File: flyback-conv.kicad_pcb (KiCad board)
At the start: 2 copper layers, 1 part

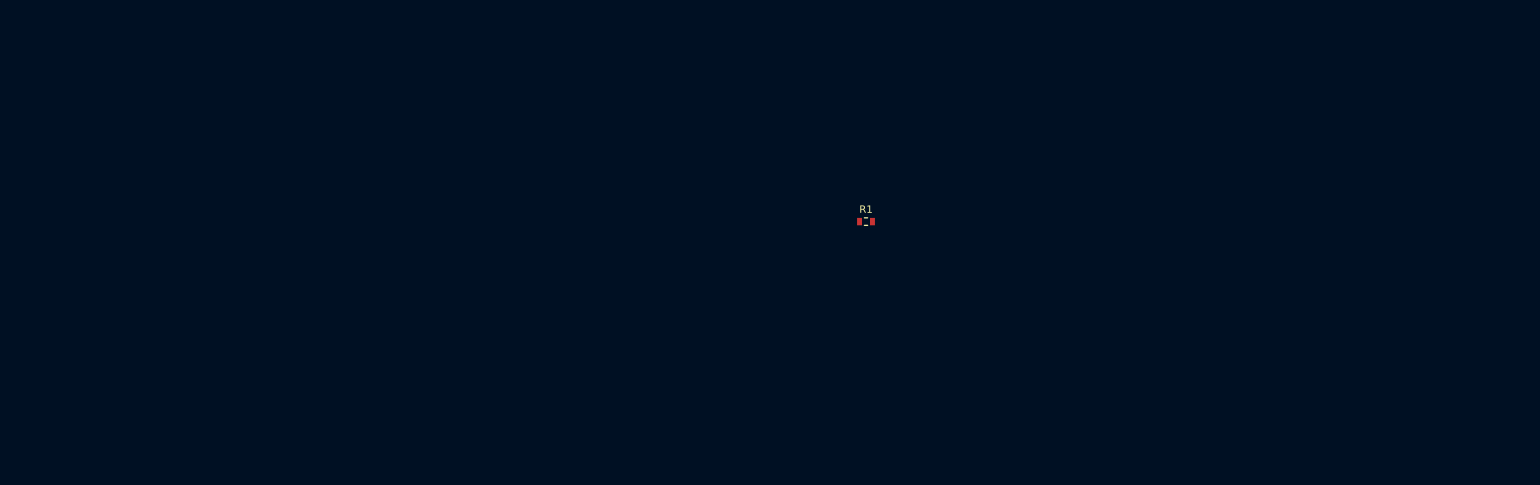
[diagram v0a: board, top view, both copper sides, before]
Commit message: fixed few lib componentes and screated PCB
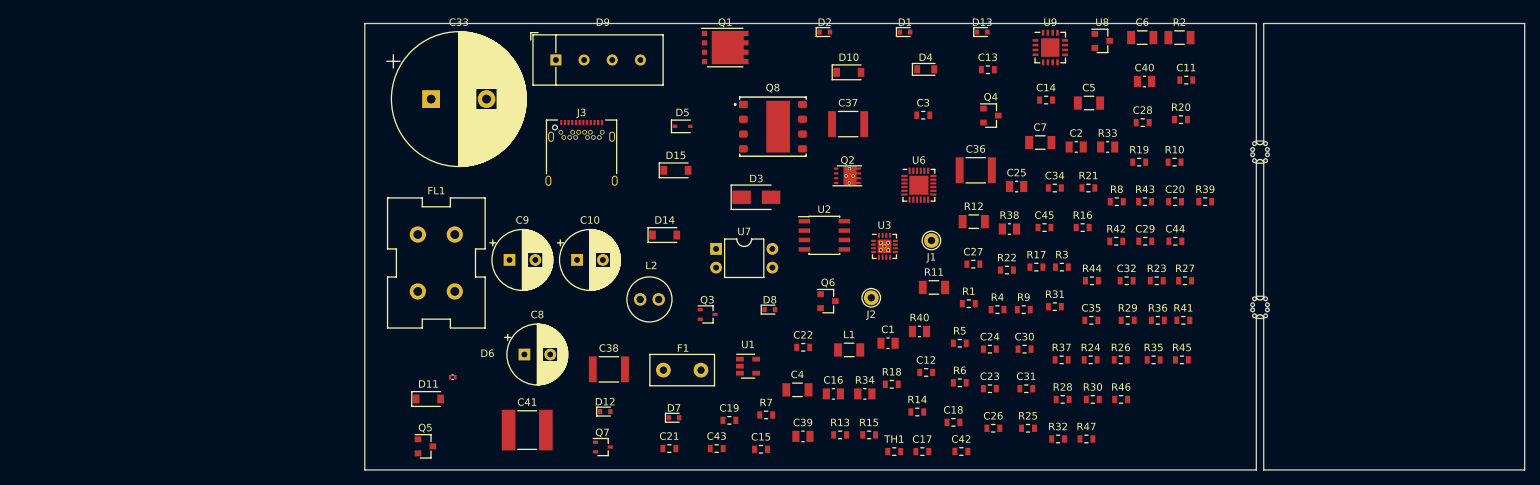
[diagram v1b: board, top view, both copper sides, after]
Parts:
- added C1: 2.2uF, Capacitor_SMD:C_0805_2012Metric, F.Cu at (173.6, 102.3)
- added C10: 270uF, Capacitor_THT:CP_Radial_D8.0mm_P3.50mm, F.Cu at (131.5, 91.0)
- added C11: 0.01uF, Capacitor_SMD:C_0603_1608Metric, F.Cu at (213.9, 66.7)
- added C12: 0.33uF, Capacitor_SMD:C_0603_1608Metric, F.Cu at (178.7, 106.2)
- added C13: 0.022uF, Capacitor_SMD:C_0603_1608Metric, F.Cu at (187.1, 65.3)
- added C14: 0.022uF, Capacitor_SMD:C_0603_1608Metric, F.Cu at (195.0, 69.4)
- added C15: 2200pF, Capacitor_SMD:C_0603_1608Metric, F.Cu at (156.4, 116.6)
- added C16: 6.8uF, Capacitor_SMD:C_0805_2012Metric, F.Cu at (166.2, 109.1)
- added C17: 12pF, Capacitor_SMD:C_0603_1608Metric, F.Cu at (178.2, 116.9)
- added C18: 22pF, Capacitor_SMD:C_0603_1608Metric, F.Cu at (182.4, 113.0)
- added C19: 0.022uF, Capacitor_SMD:C_0603_1608Metric, F.Cu at (152.1, 112.7)
- added C2: 2.2uF, Capacitor_SMD:C_0805_2012Metric, F.Cu at (199.0, 75.7)
- added C20: 3.3pF, Capacitor_SMD:C_0603_1608Metric, F.Cu at (212.4, 83.1)
- added C21: 0.022uF, Capacitor_SMD:C_0603_1608Metric, F.Cu at (144.0, 116.5)
- added C22: 0.022uF, Capacitor_SMD:C_0603_1608Metric, F.Cu at (162.1, 102.8)
- added C23: 0.1uF, Capacitor_SMD:C_0603_1608Metric, F.Cu at (187.4, 108.4)
- added C24: 0.1uF, Capacitor_SMD:C_0603_1608Metric, F.Cu at (187.4, 103.1)
- added C25: 4.7uF, Capacitor_SMD:C_0805_2012Metric, F.Cu at (191.0, 81.1)
- added C26: 0.1uF, Capacitor_SMD:C_0603_1608Metric, F.Cu at (187.8, 113.8)
- added C27: 0.01uF, Capacitor_SMD:C_0603_1608Metric, F.Cu at (185.1, 91.6)
- added C28: 0.01uF, Capacitor_SMD:C_0603_1608Metric, F.Cu at (208.0, 72.4)
- added C29: 1uF, Capacitor_SMD:C_0603_1608Metric, F.Cu at (208.4, 88.5)
- added C3: 220pF/250V, Capacitor_SMD:C_0603_1608Metric, F.Cu at (178.3, 71.4)
- added C30: 0.1uF, Capacitor_SMD:C_0603_1608Metric, F.Cu at (192.0, 103.1)
- added C31: 220pF, Capacitor_SMD:C_0603_1608Metric, F.Cu at (192.3, 108.4)
- added C32: 0.1uF, Capacitor_SMD:C_0603_1608Metric, F.Cu at (205.9, 93.8)
- added C33: 82uF, Capacitor_THT:CP_Radial_D18.0mm_P7.50mm, F.Cu at (111.8, 69.2)
- added C34: 0.22uF, Capacitor_SMD:C_0603_1608Metric, F.Cu at (196.1, 81.3)
- added C35: 220pF, Capacitor_SMD:C_0603_1608Metric, F.Cu at (201.1, 99.2)
- added C36: 0.47uF, Capacitor_SMD:C_1812_4532Metric, F.Cu at (185.4, 78.9)
- added C37: 0.22uF/500V, Capacitor_SMD:C_1812_4532Metric, F.Cu at (168.2, 72.6)
- added C38: 0.22uF/500V, Capacitor_SMD:C_1812_4532Metric, F.Cu at (135.8, 105.8)
- added C39: 0.47uF, Capacitor_SMD:C_0805_2012Metric, F.Cu at (162.1, 114.9)
- added C4: 33uF, Capacitor_SMD:C_1206_3216Metric, F.Cu at (161.3, 108.6)
- added C40: 0.47uF, Capacitor_SMD:C_0805_2012Metric, F.Cu at (208.3, 66.9)
- added C41: 2200pF/250V, Capacitor_SMD:C_2220_5650Metric, F.Cu at (124.8, 114.0)
- added C42: 560pF, Capacitor_SMD:C_0603_1608Metric, F.Cu at (183.5, 116.9)
- added C43: 4700pF, Capacitor_SMD:C_0603_1608Metric, F.Cu at (150.4, 116.5)
- added C44: 3.3pF, Capacitor_SMD:C_0603_1608Metric, F.Cu at (212.4, 88.5)
- added C45: 0.01uF, Capacitor_SMD:C_0603_1608Metric, F.Cu at (194.7, 86.6)
- added C5: 33uF, Capacitor_SMD:C_1206_3216Metric, F.Cu at (200.8, 69.8)
- added C6: 10uF, Capacitor_SMD:C_1206_3216Metric, F.Cu at (208.0, 60.9)
- added C7: 10uF, Capacitor_SMD:C_1206_3216Metric, F.Cu at (194.2, 75.1)
- added C8: 270uF, Capacitor_THT:CP_Radial_D8.0mm_P3.50mm, F.Cu at (124.4, 103.8)
- added C9: 270uF, Capacitor_THT:CP_Radial_D8.0mm_P3.50mm, F.Cu at (122.4, 91.0)
- added D1: SDM03U40-7, Diode_SMD:D_SOD-523, F.Cu at (175.9, 60.2)
- added D10: BAV21W-7-F, Diode_SMD:D_SOD-123, F.Cu at (168.3, 65.6)
- added D11: MMSZ5248B-7-F, Diode_SMD:D_SOD-123, F.Cu at (111.4, 109.8)
- added D12: CZRU52C6V2, Diode_SMD:D_SOD-523, F.Cu at (135.3, 111.5)
- added D13: CZRU52C6V2, Diode_SMD:D_SOD-523, F.Cu at (186.3, 60.2)
- added D14: CSFMT108-HF, Diode_SMD:D_SOD-123, F.Cu at (143.4, 87.6)
- added D15: CSFMT108-HF, Diode_SMD:D_SOD-123, F.Cu at (144.9, 78.9)
- added D2: BZT52C22T-7, Diode_SMD:D_SOD-523, F.Cu at (165.0, 60.2)
- added D3: B340A-13-F, Diode_SMD:D_SMA, F.Cu at (155.8, 82.5)
- added D4: RFU02VSM6S, custom-lib:TUMD2SM, F.Cu at (178.7, 65.2)
- added D5: CDSOD323-T24S, Diode_SMD:D_SOD-323, F.Cu at (145.8, 72.9)
- added D6: TPD1E05U06QDPYRQ, custom-lib:X1SON2, F.Cu at (114.7, 106.8)
- added D7: CZRU52C2, Diode_SMD:D_SOD-523, F.Cu at (144.6, 112.3)
- added D8: CZRU52C2, Diode_SMD:D_SOD-523, F.Cu at (157.6, 97.7)
- added D9: KBP06G, custom-lib:VISHAY_2KBP, F.Cu at (128.7, 63.9)
- added F1: Fuse, Fuse:Fuse_Littlefuse_395Series, F.Cu at (143.2, 105.9)
- added FL1: 20mH, Inductor_THT:L_CommonMode_Wuerth_WE-CMB-S, F.Cu at (110.0, 87.5)
- added J1: HOLE, Connector_Pin:Pin_D1.0mm_L10.0mm, F.Cu at (179.4, 88.4)
- added J2: HOLE, Connector_Pin:Pin_D1.0mm_L10.0mm, F.Cu at (171.3, 96.1)
- added J3: USB_C_Receptacle, Connector_USB:USB_C_Receptacle_Amphenol_12401548E4-2A, F.Cu at (132.1, 77.4)
- added L1: 0.68uH, Inductor_SMD:L_1206_3216Metric, F.Cu at (168.3, 103.2)
- added L2: 1uH, custom-lib:WURTH_7447462010, F.Cu at (140.1, 96.3)
- added Q1: BSC093N15NS5ATMA, Package_SON:VSONP-8-1EP_5x6_P1.27mm, F.Cu at (151.6, 62.3)
- added Q2: CSD17578Q3, custom-lib:VSONP-8-1EP_3.3x3.3_P0.65mm, F.Cu at (168.1, 79.6)
- added Q3: 2N7002KW, Package_TO_SOT_SMD:SOT-323_SC-70, F.Cu at (149.2, 98.4)
- added Q4: DMP510DL, Package_TO_SOT_SMD:SOT-23, F.Cu at (187.5, 71.5)
- added Q5: BSS126H6906, Package_TO_SOT_SMD:SOT-23, F.Cu at (111.0, 116.2)
- added Q6: MMBTA42, Package_TO_SOT_SMD:SOT-23, F.Cu at (165.5, 96.6)
- added Q7: 2N7002KW, Package_TO_SOT_SMD:SOT-323_SC-70, F.Cu at (135.0, 116.3)
- added Q8: PGA26E07, custom-lib:PANASONIC_PGA26E07BA, F.Cu at (158.0, 73.0)
- added R10: 24.9R, Resistor_SMD:R_0603_1608Metric, F.Cu at (212.3, 77.8)
- added R11: 0.18R, Resistor_SMD:R_1206_3216Metric, F.Cu at (179.8, 94.7)
- added R12: 0.005R, Resistor_SMD:R_1206_3216Metric, F.Cu at (185.2, 85.8)
- added R13: 121R, Resistor_SMD:R_0603_1608Metric, F.Cu at (167.1, 114.7)
- added R14: 2R, Resistor_SMD:R_0603_1608Metric, F.Cu at (177.5, 111.6)
- added R15: 1M, Resistor_SMD:R_0603_1608Metric, F.Cu at (171.0, 114.7)
- added R16: 69.8k, Resistor_SMD:R_0603_1608Metric, F.Cu at (199.9, 86.6)
- added R17: 10k, Resistor_SMD:R_0603_1608Metric, F.Cu at (193.6, 92.0)
- added R18: 10R, Resistor_SMD:R_0603_1608Metric, F.Cu at (174.1, 107.8)
- added R19: 82.5k, Resistor_SMD:R_0603_1608Metric, F.Cu at (207.6, 77.8)
- added R2: 22R, Resistor_SMD:R_1206_3216Metric, F.Cu at (213.0, 60.9)
- added R20: 221k, Resistor_SMD:R_0603_1608Metric, F.Cu at (213.2, 72.0)
- added R21: 0R, Resistor_SMD:R_0603_1608Metric, F.Cu at (200.7, 81.3)
- added R22: 2k, Resistor_SMD:R_0603_1608Metric, F.Cu at (189.7, 92.4)
- added R23: 10R, Resistor_SMD:R_0603_1608Metric, F.Cu at (209.9, 93.8)
- added R24: 10R, Resistor_SMD:R_0603_1608Metric, F.Cu at (201.0, 104.5)
- added R25: 61.9k, Resistor_SMD:R_0603_1608Metric, F.Cu at (192.5, 113.8)
- added R26: 90.9k, Resistor_SMD:R_0603_1608Metric, F.Cu at (205.1, 104.5)
- added R27: 191k, Resistor_SMD:R_0603_1608Metric, F.Cu at (213.8, 93.8)
- added R28: 56.2k, Resistor_SMD:R_0603_1608Metric, F.Cu at (197.2, 109.9)
- added R29: 47.5k, Resistor_SMD:R_0603_1608Metric, F.Cu at (206.0, 99.2)
- added R3: 10R, Resistor_SMD:R_0603_1608Metric, F.Cu at (197.1, 92.0)
- added R30: 27k, Resistor_SMD:R_0603_1608Metric, F.Cu at (201.3, 109.9)
- added R31: 22.1k, Resistor_SMD:R_0603_1608Metric, F.Cu at (196.2, 97.3)
- added R32: 1M, Resistor_SMD:R_0603_1608Metric, F.Cu at (196.6, 115.2)
- added R33: 1M, Resistor_SMD:R_0805_2012Metric, F.Cu at (203.3, 75.7)
- added R34: 1M, Resistor_SMD:R_0805_2012Metric, F.Cu at (170.4, 109.1)
- added R35: 100k, Resistor_SMD:R_0603_1608Metric, F.Cu at (209.5, 104.5)
- added R36: 75k, Resistor_SMD:R_0603_1608Metric, F.Cu at (210.1, 99.2)
- added R37: 100R, Resistor_SMD:R_0603_1608Metric, F.Cu at (197.1, 104.5)
- added R38: 1R, Resistor_SMD:R_0805_2012Metric, F.Cu at (190.0, 86.8)
- added R39: 0R, Resistor_SMD:R_0603_1608Metric, F.Cu at (216.5, 83.1)
- added R4: 1k, Resistor_SMD:R_0603_1608Metric, F.Cu at (188.4, 97.7)
- added R40: 1R, Resistor_SMD:R_0805_2012Metric, F.Cu at (177.8, 100.7)
- added R41: 11k, Resistor_SMD:R_0603_1608Metric, F.Cu at (213.5, 99.2)
- added R42: 562R, Resistor_SMD:R_0603_1608Metric, F.Cu at (204.5, 88.5)
- added R43: 34k, Resistor_SMD:R_0603_1608Metric, F.Cu at (208.3, 83.1)
- added R44: 60.4k, Resistor_SMD:R_0603_1608Metric, F.Cu at (201.2, 93.8)
- added R45: 10R, Resistor_SMD:R_0603_1608Metric, F.Cu at (213.3, 104.5)
- added R46: 150k, Resistor_SMD:R_0603_1608Metric, F.Cu at (205.1, 109.9)
- added R47: 150k, Resistor_SMD:R_0603_1608Metric, F.Cu at (200.4, 115.2)
- added R5: 10R, Resistor_SMD:R_0603_1608Metric, F.Cu at (183.3, 102.3)
- added R6: 10R, Resistor_SMD:R_0603_1608Metric, F.Cu at (183.3, 107.6)
- added R7: 10k, Resistor_SMD:R_0603_1608Metric, F.Cu at (157.1, 112.0)
- added R8: 100k, Resistor_SMD:R_0603_1608Metric, F.Cu at (204.5, 83.1)
- added R9: 1.6k, Resistor_SMD:R_0603_1608Metric, F.Cu at (191.9, 97.7)
- added TH1: 47k, Resistor_SMD:R_0603_1608Metric, F.Cu at (174.4, 116.9)
- added U1: UCC24612, Package_TO_SOT_SMD:SOT-23-5, F.Cu at (154.6, 105.4)
- added U2: ISO7710, Package_SO:SOIC-8_3.9x4.9mm_P1.27mm, F.Cu at (165.0, 87.7)
- added U3: UCC28780, Package_DFN_QFN:QFN-16-1EP_3x3mm_P0.5mm_EP2.7x2.7mm_ThermalVias, F.Cu at (173.1, 89.2)
- added U6: TPS25740B, Package_DFN_QFN:QFN-24-1EP_4x4mm_P0.5mm_EP2.6x2.6mm, F.Cu at (177.8, 80.9)
- added U7: SFH617A-1, Package_DIP:DIP-4_W7.62mm, F.Cu at (150.3, 89.5)
- added U8: ATL431, Package_TO_SOT_SMD:SOT-23, F.Cu at (202.5, 61.4)
- added U9: AN34092B, Package_DFN_QFN:QFN-16-1EP_4x4mm_P0.65mm_EP2.5x2.5mm, F.Cu at (195.5, 62.3)
- added mouse-bite-1mm-slot: VAL**, custom-lib:mouse-bite-1mm-slot, F.Cu at (223.9, 97.4)
- added mouse-bite-1mm-slot: VAL**, custom-lib:mouse-bite-1mm-slot, F.Cu at (223.9, 76.4)
- R1: value 20k -> 100R
- moved R1 17.8 mm to (184.5, 96.9)
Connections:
- R1 pad 1: Net-(R1-Pad1) -> /F
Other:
- board outline added: 156.9 x 60.4 mm

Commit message: generated BOM v1.0, added some screenshots and added an alternative for the transformer
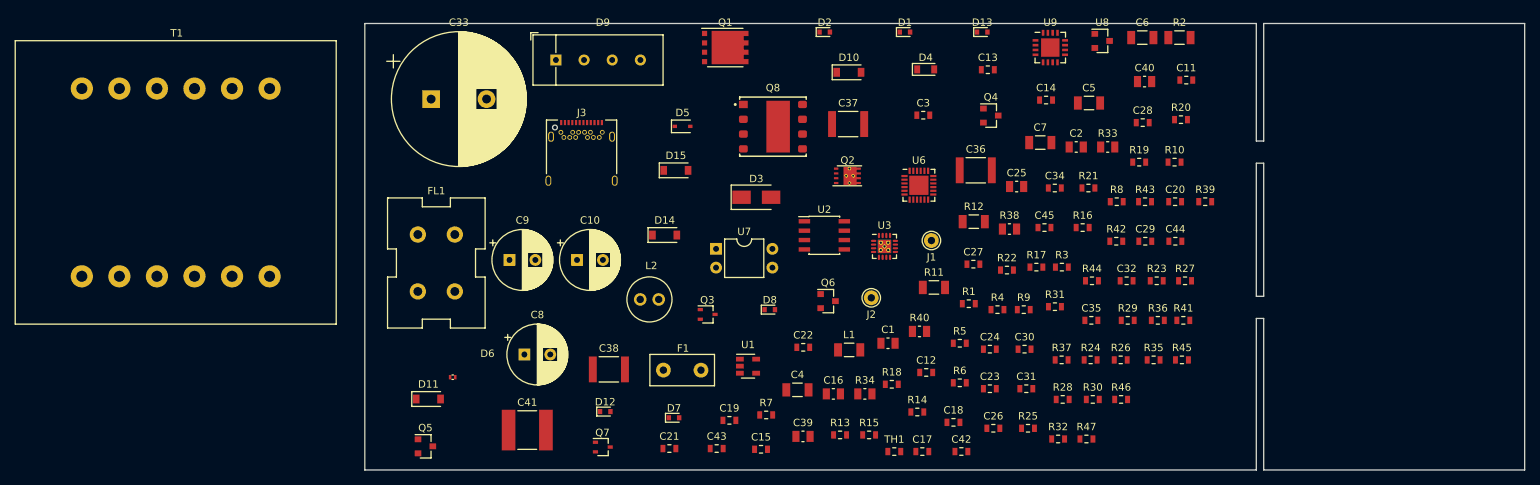
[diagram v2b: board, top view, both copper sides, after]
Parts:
- removed mouse-bite-1mm-slot (x2): VAL**, custom-lib:mouse-bite-1mm-slot
- added T1: 150-2670, Transformer_THT:Transformer_37x44, F.Cu at (69.6, 67.8)
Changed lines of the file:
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@@
   (general
     (thickness 1.6)
-    (drawings 17)
+    (drawings 18)
     (tracks 0)
     (zones 0)
-    (modules 132)
+    (modules 131)
     (nets 124)
   )
@@
     (add_net "Net-(U9-Pad9)")
   )
+  (module Transformer_THT:Transformer_37x44 (layer F.Cu)
+    (at 69.6 67.8)
+    (descr "transformer 37x44mm²")
+    (tags "transformer 37x44mm²")
+    (fp_text reference T1 (at 7.75 -7.5) (layer F.SilkS)
+      (effects (font (size 1 1) (thickness 0.15)))
+    )
+    (fp_text value 150-2670 (at 7.25 14.5) (layer F.Fab)
+      (effects (font (size 1 1) (thickness 0.15)))
+    )
+    (fp_text user %R (at 7.62 12.7) (layer F.Fab)
+      (effects (font (size 1 1) (thickness 0.15)))
+    )
+    (fp_line (start -6.99 1.27) (end 22.23 1.27) (layer F.Fab) (width 0.1))
+    (fp_line (start 22.23 1.27) (end 22.23 24.13) (layer F.Fab) (width 0.1))
+    (fp_line (start 22.23 24.13) (end -6.99 24.13) (layer F.Fab) (width 0.1))
+    (fp_line (start -6.99 24.13) (end -6.99 1.27) (layer F.Fab) (width 0.1))
+    (fp_line (start -13.97 -6.35) (end 29.21 -6.35) (layer F.Fab) (width 0.1))
+    (fp_line (start 29.21 -6.35) (end 29.21 31.75) (layer F.Fab) (width 0.1))
+    (fp_line (start 29.21 31.75) (end -13.97 31.75) (layer F.Fab) (width 0.1))
+    (fp_line (start -13.97 31.75) (end -13.97 -6.35) (layer F.Fab) (width 0.1))
+    (fp_line (start -14.22 -6.6) (end 29.46 -6.6) (layer F.CrtYd) (width 0.05))
+    (fp_line (start -14.22 -6.6) (end -14.22 32) (layer F.CrtYd) (width 0.05))
+    (fp_line (start 29.46 32) (end 29.46 -6.6) (layer F.CrtYd) (width 0.05))
+    (fp_line (start 29.46 32) (end -14.22 32) (layer F.CrtYd) (width 0.05))
+    (fp_line (start -14.09 -6.47) (end 29.33 -6.47) (layer F.SilkS) (width 0.12))
+    (fp_line (start -14.09 -6.47) (end -14.09 31.87) (layer F.SilkS) (width 0.12))
+    (fp_line (start 29.33 31.87) (end 29.33 -6.47) (layer F.SilkS) (width 0.12))
+    (fp_line (start 29.33 31.87) (end -14.09 31.87) (layer F.SilkS) (width 0.12))
+    (pad 2 thru_hole circle (at 20.32 0) (size 3 3) (drill 1.5) (layers *.Cu *.Mask)
+      (net 76 /VSW))
+    (pad 4 thru_hole circle (at -5.08 25.4) (size 3 3) (drill 1.5) (layers *.Cu *.Mask)
+      (net 8 Earth))
+    (pad 3 thru_hole circle (at 5.08 25.4) (size 3 3) (drill 1.5) (layers *.Cu *.Mask)
+      (net 58 /VS))
+    (pad 1 thru_hole circle (at 0 0) (size 3 3) (drill 1.5) (layers *.Cu *.Mask)
+      (net 11 "Net-(C33-Pad1)"))
+    (pad "" thru_hole circle (at -5.08 0) (size 3 3) (drill 1.5) (layers *.Cu *.Mask))
+    (pad "" thru_hole circle (at 5.08 0) (size 3 3) (drill 1.5) (layers *.Cu *.Mask))
+    (pad "" thru_hole circle (at 10.16 0) (size 3 3) (drill 1.5) (layers *.Cu *.Mask))
+    (pad "" thru_hole circle (at 15.24 0) (size 3 3) (drill 1.5) (layers *.Cu *.Mask))
+    (pad "" thru_hole circle (at 0 25.4) (size 3 3) (drill 1.5) (layers *.Cu *.Mask))
+    (pad "" thru_hole circle (at 10.16 25.4) (size 3 3) (drill 1.5) (layers *.Cu *.Mask))
+    (pad "" thru_hole circle (at 15.24 25.4) (size 3 3) (drill 1.5) (layers *.Cu *.Mask))
+    (pad "" thru_hole circle (at 20.32 25.4) (size 3 3) (drill 1.5) (layers *.Cu *.Mask))
+    (model ${KISYS3DMOD}/Transformer_THT.3dshapes/Transformer_37x44.wrl
+      (at (xyz 0 0 0))
+      (scale (xyz 1 1 1))
+      (rotate (xyz 0 0 0))
+    )
+    (model ${KIPRJMOD}/LIB/3D/070-4869.STEP
+      (offset (xyz -8 -28.5 0.5))
+      (scale (xyz 1 1 1))
+      (rotate (xyz -90 0 90))
+    )
+  )
   (module Capacitor_SMD:C_0603_1608Metric (layer F.Cu)
     (at 178.742619 106.2075)
@@
       (net 3 /CC2))
   )
-  (module custom-lib:mouse-bite-1mm-slot (layer F.Cu)
-    (at 223.9 97.4 90)
-    (fp_text reference mouse-bite-1mm-slot (at 0 -2 90) (layer F.SilkS) hide
-      (effects (font (size 1 1) (thickness 0.2)))
-    )
-    (fp_text value VAL** (at 0 2.1 90) (layer F.SilkS) hide
-      (effects (font (size 1 1) (thickness 0.2)))
-    )
-    (fp_line (start 1.5 0) (end 1.5 0) (layer Eco1.User) (width 1))
-    (fp_line (start -1.5 0) (end -1.5 0) (layer Eco1.User) (width 1))
-    (fp_arc (start -1.5 0) (end -1.5 -0.5) (angle 180) (layer F.SilkS) (width 0.1))
-    (fp_arc (start 1.5 0) (end 1.5 0.5) (angle 180) (layer F.SilkS) (width 0.1))
-    (fp_circle (center -1.5 0) (end -1.44 0) (layer Dwgs.User) (width 0.05))
-    (fp_circle (center 1.5 0) (end 1.56 0) (layer Dwgs.User) (width 0.05))
-    (pad "" np_thru_hole circle (at 0.35 1 90) (size 0.5 0.5) (drill 0.5) (layers *.Cu *.Mask))
-    (pad "" np_thru_hole circle (at -0.35 1 90) (size 0.5 0.5) (drill 0.5) (layers *.Cu *.Mask))
-    (pad "" np_thru_hole circle (at 1.15 -0.75 90) (size 0.5 0.5) (drill 0.5) (layers *.Cu *.Mask))
-    (pad "" np_thru_hole circle (at -0.35 -1 90) (size 0.5 0.5) (drill 0.5) (layers *.Cu *.Mask))
-    (pad "" np_thru_hole circle (at -1.15 -0.75 90) (size 0.5 0.5) (drill 0.5) (layers *.Cu *.Mask))
-    (pad "" np_thru_hole circle (at 1.15 0.75 90) (size 0.5 0.5) (drill 0.5) (layers *.Cu *.Mask))
-    (pad "" np_thru_hole circle (at -1.15 0.75 90) (size 0.5 0.5) (drill 0.5) (layers *.Cu *.Mask))
-    (pad "" np_thru_hole circle (at 0.35 -1 90) (size 0.5 0.5) (drill 0.5) (layers *.Cu *.Mask))
-  )
-  (module custom-lib:mouse-bite-1mm-slot (layer F.Cu)
-    (at 223.9 76.4 90)
-    (fp_text reference mouse-bite-1mm-slot (at 0 -2 90) (layer F.SilkS) hide
-      (effects (font (size 1 1) (thickness 0.2)))
-    )
-    (fp_text value VAL** (at 0 2.1 90) (layer F.SilkS) hide
-      (effects (font (size 1 1) (thickness 0.2)))
-    )
-    (fp_line (start 1.5 0) (end 1.5 0) (layer Eco1.User) (width 1))
-    (fp_line (start -1.5 0) (end -1.5 0) (layer Eco1.User) (width 1))
-    (fp_arc (start -1.5 0) (end -1.5 -0.5) (angle 180) (layer F.SilkS) (width 0.1))
-    (fp_arc (start 1.5 0) (end 1.5 0.5) (angle 180) (layer F.SilkS) (width 0.1))
-    (fp_circle (center -1.5 0) (end -1.44 0) (layer Dwgs.User) (width 0.05))
-    (fp_circle (center 1.5 0) (end 1.56 0) (layer Dwgs.User) (width 0.05))
-    (pad "" np_thru_hole circle (at 0.35 1 90) (size 0.5 0.5) (drill 0.5) (layers *.Cu *.Mask))
-    (pad "" np_thru_hole circle (at -0.35 1 90) (size 0.5 0.5) (drill 0.5) (layers *.Cu *.Mask))
-    (pad "" np_thru_hole circle (at 1.15 -0.75 90) (size 0.5 0.5) (drill 0.5) (layers *.Cu *.Mask))
-    (pad "" np_thru_hole circle (at -0.35 -1 90) (size 0.5 0.5) (drill 0.5) (layers *.Cu *.Mask))
-    (pad "" np_thru_hole circle (at -1.15 -0.75 90) (size 0.5 0.5) (drill 0.5) (layers *.Cu *.Mask))
-    (pad "" np_thru_hole circle (at 1.15 0.75 90) (size 0.5 0.5) (drill 0.5) (layers *.Cu *.Mask))
-    (pad "" np_thru_hole circle (at -1.15 0.75 90) (size 0.5 0.5) (drill 0.5) (layers *.Cu *.Mask))
-    (pad "" np_thru_hole circle (at 0.35 -1 90) (size 0.5 0.5) (drill 0.5) (layers *.Cu *.Mask))
+  (dimension 120.600166 (width 0.3) (layer Eco2.User)
+    (gr_text "120.600 mm" (at 163.083665 138.649974 -0.09501778937) (layer Eco2.User)
+      (effects (font (size 1.5 1.5) (thickness 0.3)))
+    )
+    (feature1 (pts (xy 102.8 128.7) (xy 102.781426 139.899972)))
+    (feature2 (pts (xy 223.4 128.9) (xy 223.381426 140.099972)))
+    (crossbar (pts (xy 223.385904 137.399976) (xy 102.785904 137.199976)))
+    (arrow1a (pts (xy 102.785904 137.199976) (xy 103.913379 136.615424)))
+    (arrow1b (pts (xy 102.785904 137.199976) (xy 103.911434 137.788264)))
+    (arrow2a (pts (xy 223.385904 137.399976) (xy 222.260374 136.811688)))
+    (arrow2b (pts (xy 223.385904 137.399976) (xy 222.258429 137.984528)))
   )
   (gr_line (start 224.4 74.9) (end 223.4 74.9) (layer Edge.Cuts) (width 0.15))
